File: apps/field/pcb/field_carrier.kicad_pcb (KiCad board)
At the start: 2 copper layers, 55 x 46 mm, 14 parts, among them J1 XIAO_ESP32C6, J3 E220_EV2, J4 ログ_UART0

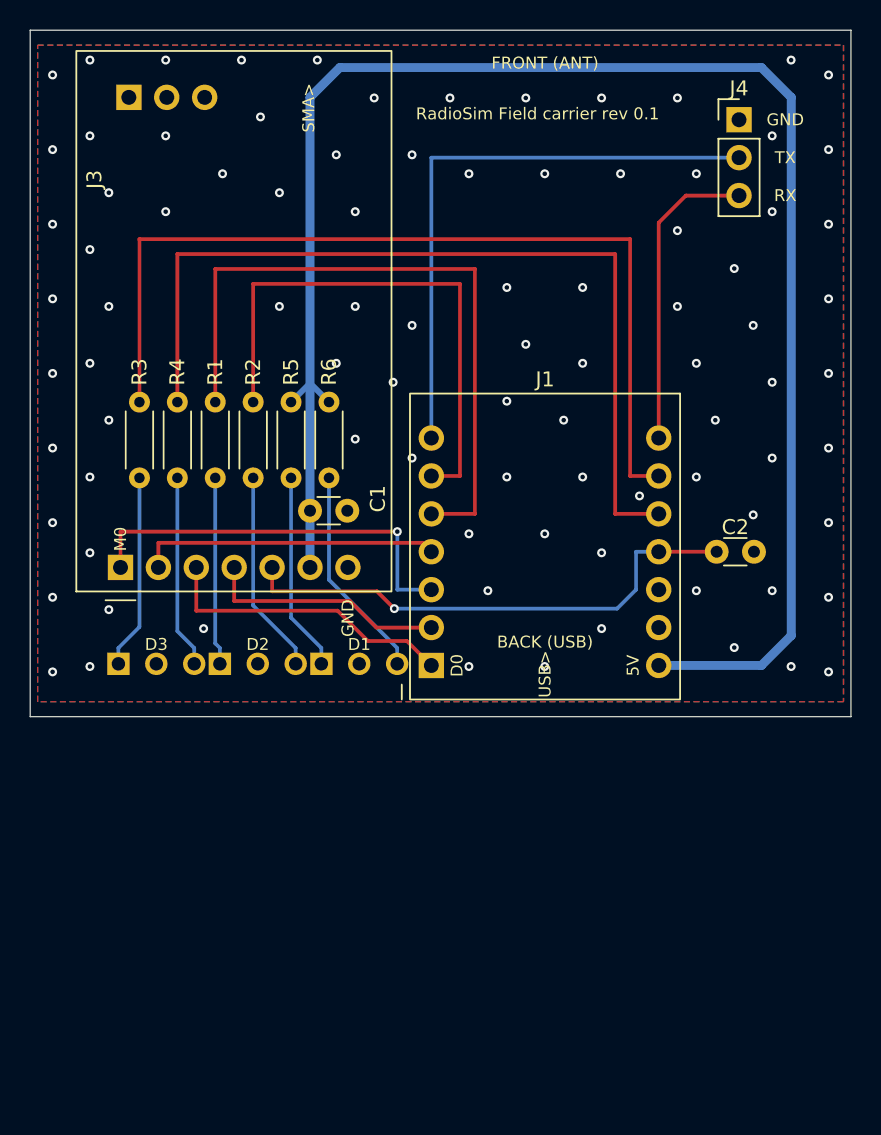
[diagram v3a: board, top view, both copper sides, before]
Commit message: fix(field): 台を JLCPCB の公差に合わせる（長さ 45.8＝前の縁を 0.2 控える・シルクを高さ 1.0／線 0.15 へ）
- 外形の公差 ±0.2（JLCPCB 標準）で 46.0 ちょうどだと太った個体が前後のパネルに入らない
  ＝前の縁だけ 0 → 0.2（後端 46.0 は背面パネルの基準なので残す）。溝の帯のレジスト抜きも前を 0.7 へ
- シルクを全部 高さ 1.0・線 0.15（JLCPCB が判読できるとする下限）へ。.kicad_pro の
  min_text_height／min_text_thickness も同じ値にして DRC が以後止める
- 重なりを避けて基板名を 2 行で右上へ・BACK (USB)・USB>・LED の記号を移し、XIAO の枠を ±8.93 へ
  （D1 のパッドとの間 0.035 だった）。シルクとパッドの間 ≥0.15 を全数で確認
- XIAO のフットプリントの説明の「0.5 はみ出す」（台が 45.0 の頃の値）を直した
- DRC〔照合つき〕0・未接続 0

Co-Authored-By: Claude Opus 5.5 <noreply@anthropic.com>
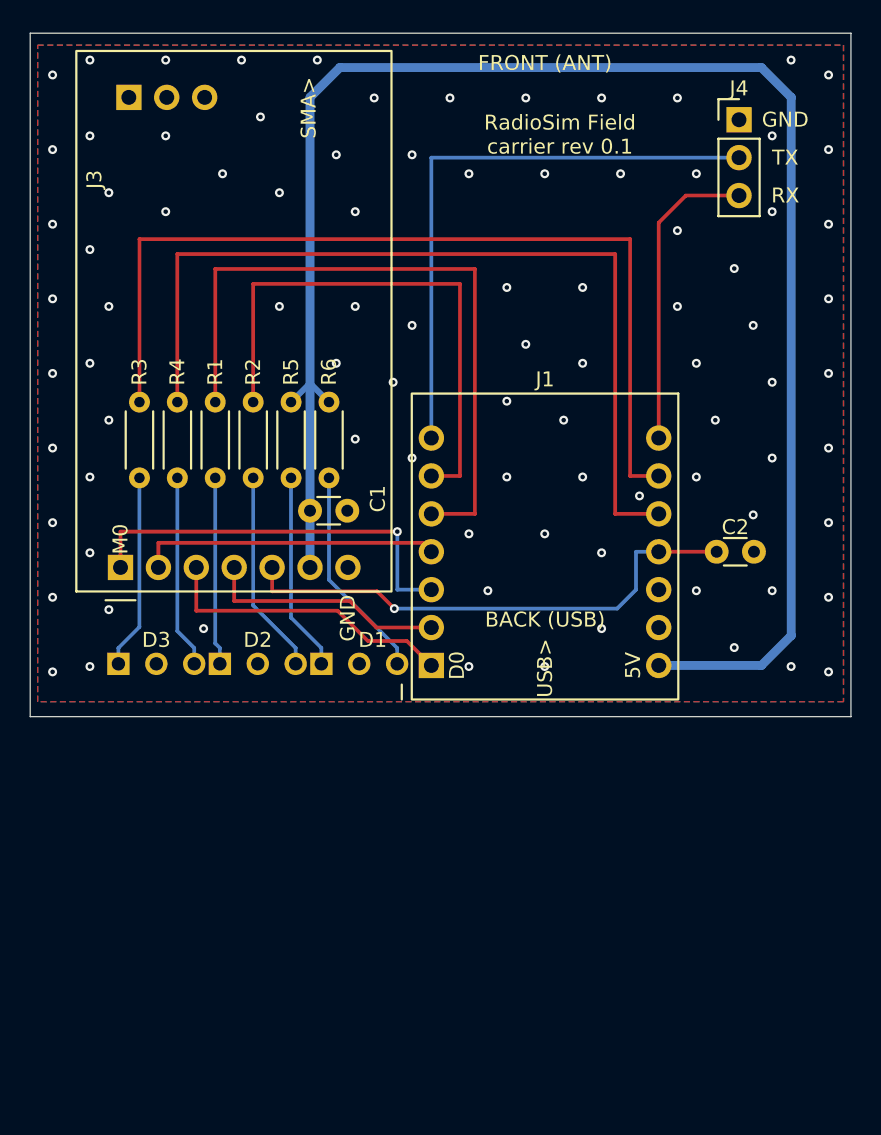
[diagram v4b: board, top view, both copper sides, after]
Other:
- board size 55 x 46 mm -> 55 x 45.8 mm
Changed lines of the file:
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@@
 			(end 0 -1.38)
 			(stroke
-				(width 0.12)
+				(width 0.15)
 				(type solid)
 			)
@@
 			(end -1.38 -1.38)
 			(stroke
-				(width 0.12)
+				(width 0.15)
 				(type solid)
 			)
@@
 			(end -1.38 6.46)
 			(stroke
-				(width 0.12)
+				(width 0.15)
 				(type solid)
 			)
@@
 			(end 1.38 1.27)
 			(stroke
-				(width 0.12)
+				(width 0.15)
 				(type solid)
 			)
@@
 			(end 1.38 6.46)
 			(stroke
-				(width 0.12)
+				(width 0.15)
 				(type solid)
 			)
@@
 			(end 1.38 6.46)
 			(stroke
-				(width 0.12)
+				(width 0.15)
 				(type solid)
 			)
@@
 			(end 4.46 0.92)
 			(stroke
-				(width 0.12)
+				(width 0.15)
 				(type solid)
 			)
@@
 			(end 4.46 -0.92)
 			(stroke
-				(width 0.12)
+				(width 0.15)
 				(type solid)
 			)
@@
 			(end 2.015 -0.92)
 			(stroke
-				(width 0.12)
+				(width 0.15)
 				(type solid)
 			)
@@
 			(end 0.485 0.92)
 			(stroke
-				(width 0.12)
+				(width 0.15)
 				(type solid)
 			)
@@
 		(tags "LED 3mm horizontal bicolor common cathode")
 		(property "Reference" "D1"
-			(at 0 -1.3 0)
-			(layer "F.SilkS")
-			(effects
-				(font
-					(size 0.8 0.8)
-					(thickness 0.12)
+			(at 0.9 -1.6 0)
+			(layer "F.SilkS")
+			(effects
+				(font
+					(size 1 1)
+					(thickness 0.15)
 				)
 			)
@@
 			(end 2.015 -0.92)
 			(stroke
-				(width 0.12)
+				(width 0.15)
 				(type solid)
 			)
@@
 			(end 0.485 0.92)
 			(stroke
-				(width 0.12)
+				(width 0.15)
 				(type solid)
 			)
@@
 		(tags "LED 3mm horizontal bicolor common cathode")
 		(property "Reference" "D3"
-			(at 0 -1.3 0)
-			(layer "F.SilkS")
-			(effects
-				(font
-					(size 0.8 0.8)
-					(thickness 0.12)
+			(at 0 -1.6 0)
+			(layer "F.SilkS")
+			(effects
+				(font
+					(size 1 1)
+					(thickness 0.15)
 				)
 			)
@@
 		(tags "LED 3mm horizontal bicolor common cathode")
 		(property "Reference" "D2"
-			(at 0 -1.3 0)
-			(layer "F.SilkS")
-			(effects
-				(font
-					(size 0.8 0.8)
-					(thickness 0.12)
+			(at 0 -1.6 0)
+			(layer "F.SilkS")
+			(effects
+				(font
+					(size 1 1)
+					(thickness 0.15)
 				)
 			)
@@
 			(end 4.46 0.92)
 			(stroke
-				(width 0.12)
+				(width 0.15)
 				(type solid)
 			)
@@
 			(end 4.46 -0.92)
 			(stroke
-				(width 0.12)
+				(width 0.15)
 				(type solid)
 			)
@@
 			(end 4.46 0.92)
 			(stroke
-				(width 0.12)
+				(width 0.15)
 				(type solid)
 			)
@@
 			(end 4.46 -0.92)
 			(stroke
-				(width 0.12)
+				(width 0.15)
 				(type solid)
 			)
@@
 			(end 4.46 0.92)
 			(stroke
-				(width 0.12)
+				(width 0.15)
 				(type solid)
 			)
@@
 			(end 4.46 -0.92)
 			(stroke
-				(width 0.12)
+				(width 0.15)
 				(type solid)
 			)
@@
 			(end 4.46 0.92)
 			(stroke
-				(width 0.12)
+				(width 0.15)
 				(type solid)
 			)
@@
 			(end 4.46 -0.92)
 			(stroke
-				(width 0.12)
+				(width 0.15)
 				(type solid)
 			)
@@
 			(end 8.9 9.6)
 			(stroke
-				(width 0.12)
-				(type solid)
-			)
-			(layer "F.SilkS")
-		)
-		(fp_rect
-			(start -10.6 -9.05)
-			(end 9.9 9.05)
-			(stroke
-				(width 0.12)
+				(width 0.15)
+				(type solid)
+			)
+			(layer "F.SilkS")
+		)
+		(fp_rect
+			(start -10.6 -8.93)
+			(end 9.9 8.93)
+			(stroke
+				(width 0.15)
 				(type solid)
 			)
@@
 			(effects
 				(font
-					(size 0.8 0.8)
-					(thickness 0.12)
+					(size 1 1)
+					(thickness 0.15)
 				)
 			)
 		)
 		(fp_text user "USB>"
-			(at 8.2 0 270)
-			(layer "F.SilkS")
-			(effects
-				(font
-					(size 0.8 0.8)
-					(thickness 0.12)
+			(at 7.8 0 270)
+			(layer "F.SilkS")
+			(effects
+				(font
+					(size 1 1)
+					(thickness 0.15)
 				)
 			)
@@
 			(effects
 				(font
-					(size 0.8 0.8)
-					(thickness 0.12)
+					(size 1 1)
+					(thickness 0.15)
 				)
 			)
@@
 			(end -2.2 1)
 			(stroke
-				(width 0.12)
+				(width 0.15)
 				(type solid)
 			)
@@
 			(end 34.61 18.16)
 			(stroke
-				(width 0.12)
+				(width 0.15)
 				(type solid)
 			)
@@
 			(effects
 				(font
-					(size 0.8 0.8)
-					(thickness 0.12)
+					(size 1 1)
+					(thickness 0.15)
 				)
 			)
@@
 			(effects
 				(font
-					(size 0.8 0.8)
-					(thickness 0.12)
+					(size 1 1)
+					(thickness 0.15)
 				)
 			)
@@
 			(effects
 				(font
-					(size 0.8 0.8)
-					(thickness 0.12)
+					(size 1 1)
+					(thickness 0.15)
 				)
 			)
@@
 			(end 4.46 0.92)
 			(stroke
-				(width 0.12)
+				(width 0.15)
 				(type solid)
 			)
@@
 			(end 4.46 -0.92)
 			(stroke
-				(width 0.12)
+				(width 0.15)
 				(type solid)
 			)
@@
 	)
 	(gr_rect
-		(start 50.5 30.5)
+		(start 50.5 30.7)
 		(end 52.5 75.5)
 		(stroke
@@
 	)
 	(gr_rect
-		(start 102.5 30.5)
+		(start 102.5 30.7)
 		(end 104.5 75.5)
 		(stroke
@@
 	)
 	(gr_rect
-		(start 50.5 30.5)
+		(start 50.5 30.7)
 		(end 52.5 75.5)
 		(stroke
@@
 	)
 	(gr_rect
-		(start 102.5 30.5)
+		(start 102.5 30.7)
 		(end 104.5 75.5)
 		(stroke
@@
 	)
 	(gr_line
-		(start 50 30)
-		(end 105 30)
+		(start 50 30.2)
+		(end 105 30.2)
 		(stroke
 			(width 0.05)
@@
 	(gr_line
 		(start 50 76)
-		(end 50 30)
+		(end 50 30.2)
 		(stroke
 			(width 0.05)
@@
 	)
 	(gr_line
-		(start 105 30)
+		(start 105 30.2)
 		(end 105 76)
 		(stroke
@@
 		(layer "Edge.Cuts")
 	)
-	(gr_text "RadioSim Field carrier rev 0.1"
-		(at 84 35.6 0)
-		(layer "F.SilkS")
-		(effects
-			(font
-				(size 0.8 0.8)
-				(thickness 0.12)
-			)
-		)
-	)
 	(gr_text "FRONT (ANT)"
 		(at 84.5 32.2 0)
@@
 		(effects
 			(font
-				(size 0.8 0.8)
-				(thickness 0.12)
+				(size 1 1)
+				(thickness 0.15)
 			)
 		)
 	)
 	(gr_text "BACK (USB)"
-		(at 84.5 71 0)
+		(at 84.5 69.5 0)
 		(layer "F.SilkS")
 		(effects
 			(font
-				(size 0.8 0.8)
-				(thickness 0.12)
+				(size 1 1)
+				(thickness 0.15)
+			)
+		)
+	)
+	(gr_text "RadioSim Field\ncarrier rev 0.1"
+		(at 85.5 37 0)
+		(layer "F.SilkS")
+		(effects
+			(font
+				(size 1 1)
+				(thickness 0.15)
 			)
 		)
@@
 		(effects
 			(font
-				(size 0.8 0.8)
-				(thickness 0.12)
+				(size 1 1)
+				(thickness 0.15)
 			)
 		)
@@
 		(effects
 			(font
-				(size 0.8 0.8)
-				(thickness 0.12)
+				(size 1 1)
+				(thickness 0.15)
 			)
 		)
@@
 		(effects
 			(font
-				(size 0.8 0.8)
-				(thickness 0.12)
+				(size 1 1)
+				(thickness 0.15)
 			)
 		)
@@
 		(effects
 			(font
-				(size 0.8 0.8)
-				(thickness 0.12)
+				(size 1 1)
+				(thickness 0.15)
 			)
 			(justify mirror)

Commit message: feat(field): 台の裏のシルクに JLCPCB の発注番号の位置（JLCJLCJLCJLC）を足す
基板名の下（台の x 28.7〜39.3・y 7.0〜8.7）に、基板名と同じ高さ 1.0・線 0.15・鏡像で置いた。
発注画面で「位置を指定」を選ぶと、ここに番号が入る。DRC（照合つき）0・未配線 0・不一致 0。

Co-Authored-By: Claude Opus 5.5 <noreply@anthropic.com>
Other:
- board text added: "JLCJLCJLCJLC"
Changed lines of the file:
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@@
+		)
+	)
+	(gr_text "JLCJLCJLCJLC"
+		(at 84 37.8 0)
+		(layer "B.SilkS")
+		(effects
+			(font
+				(size 1 1)
+				(thickness 0.15)
+			)
+			(justify mirror)
 		)
 	)

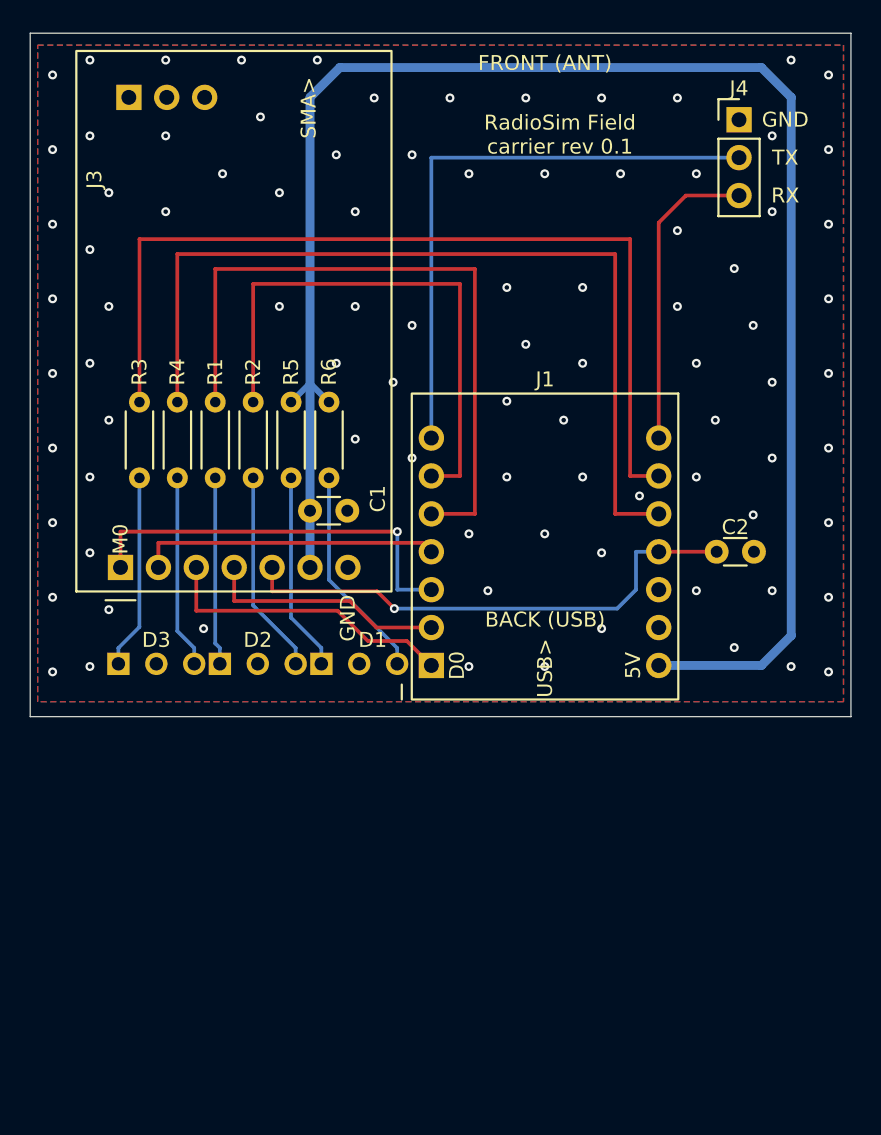
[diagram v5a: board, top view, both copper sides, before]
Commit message: fix(field): XIAO を 4.0 mm 前へ動かし、USB ケーブルの胴を背面パネルの穴に 1.45 mm 入れる
- 実測（2026-10-21）＝ケーブルを奥まで挿すと胴の先端は XIAO の基板の縁から 4.6 mm
  （受け口の面より 2.6 mm 先）。受け口を外面と面一にした前の配置では胴がパネルの外 2.55 mm で止まり、
  胴に合わせた穴（12.8×7.6）がこじる力を受けていなかった
- J1（XIAO）と C2 を y −4.0。XIAO の縁は台の後端から 4.55 mm 内側・胴の先端は 46.05
  （パネルの内面 46.0・外面 47.5）
- XIAO につながる線を引き直した。M0 は表だけで届く・M1 にビアを 1 つ・AUX のビアは
  J3 の GND ピンの裏のサーマルを 2 本残す位置（23.0, 37.6）へ。ぶつかる縫いビア 4 つを除いた
- BACK (USB) のシルクを XIAO の後ろ（y 43.5）へ。HARDWARE.md の「止め方」に配置の理由を書いた
- DRC〔照合つき〕0・未配線 0・不一致 0。穴から線 0.35／穴どうし 0.45 に締めた写しでも 0
- 同じ回で当てた残り 2 点は合っていた＝EV2 の SMA のねじはパネルの外に 9.5 mm 出る・
  GND の 3 穴は 2.54 間隔のピンヘッダが入る

Co-Authored-By: Claude Opus 5.5 <noreply@anthropic.com>
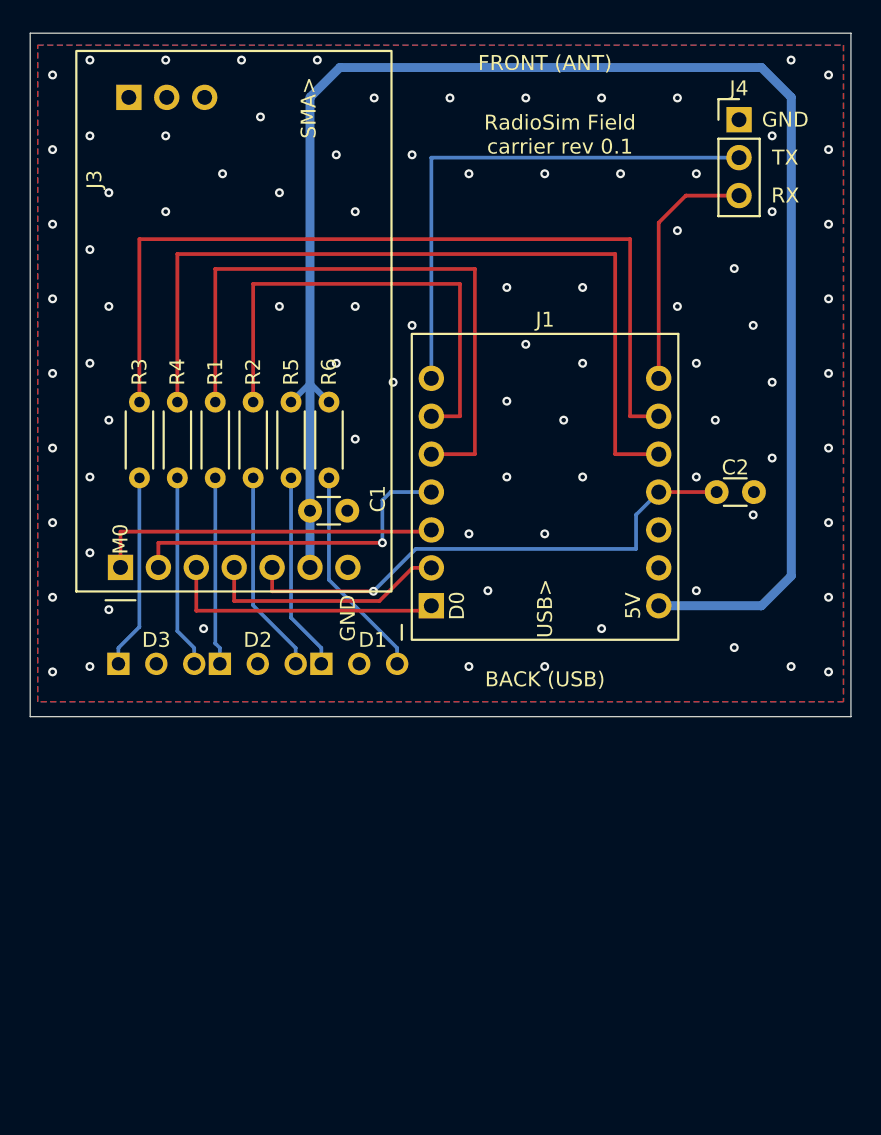
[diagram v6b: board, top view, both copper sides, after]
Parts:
- moved C2 4.00 mm to (96.0, 61.0)
- moved J1 4.00 mm to (84.5, 61.0)
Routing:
- net +5V: track 114.8 -> 110.8 mm
- net /LOG_TX: track 39.4 -> 35.4 mm
- net /LOG_RX: track 20.6 -> 16.6 mm
- net /LED920_TX: track 45.6 -> 41.6 mm
- net /LED920_RX: track 36.6 -> 32.6 mm
- net /LED24_TX: track 61.6 -> 57.6 mm
- net /LED24_RX: track 59.6 -> 55.6 mm
- net /EV2_M0: track 27.1 -> 23.3 mm, vias 1 -> 0
- net /EV2_M1: track 20.2 -> 23.0 mm, vias 0 -> 1
- net /EV2_RXD: track 20.2 -> 18.8 mm
- net /EV2_AUX: track 34.9 -> 35.5 mm
- net GND: vias 90 -> 86
